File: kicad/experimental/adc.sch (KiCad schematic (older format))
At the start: 3 parts

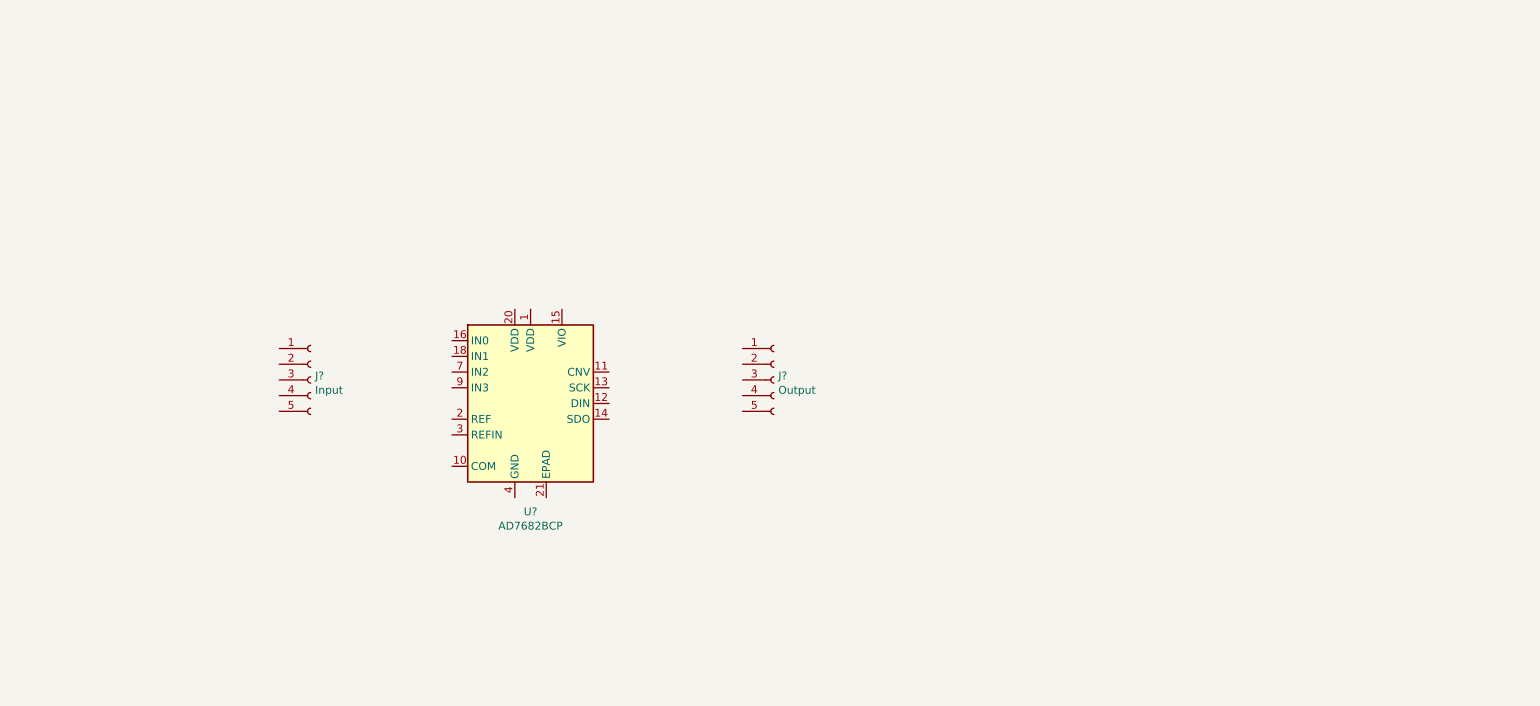
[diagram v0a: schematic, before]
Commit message: created schematic for experimental adc
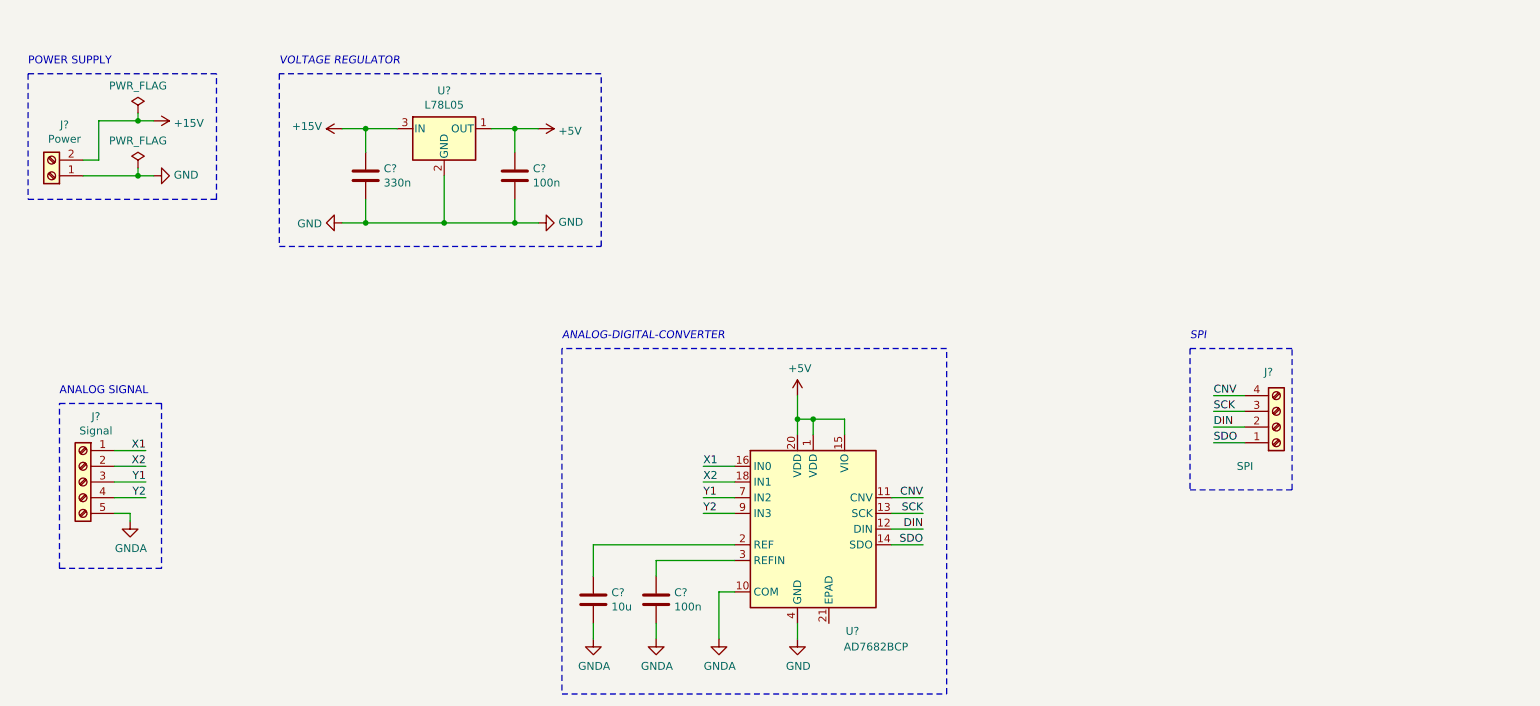
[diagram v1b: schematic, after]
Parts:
- removed J?: Input, symbol Connector:Conn_01x05_Female
- removed J?: Output, symbol Connector:Conn_01x05_Female
- added C?: 330n, symbol Device:C
- added C? (x2): 100n, symbol Device:C
- added C?: 10u, symbol Device:C
- added J?: SPI, symbol Connector:Screw_Terminal_01x04
- added J?: Signal, symbol Connector:Screw_Terminal_01x05
- added J?: Power, symbol Connector:Screw_Terminal_01x02
- added U?: L78L05, Package_TO_SOT_SMD:SOT-89-3, symbol Regulator_Linear:L78L05_SOT89
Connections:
- net +5V: now reaches U?.1 (VDD)
- net +5V: now also U?.15 (VIO), U?.20 (VDD), C?.1, U?.1 (OUT)
- net GNDA: now reaches U?.10 (COM)
- net GNDA: now also C?.2, C?.2, J?.5 (Pin_5)
- net CNV: now reaches U?.11 (CNV)
- net CNV: now also J?.4 (Pin_4)
- net DIN: now reaches U?.12 (DIN)
- net DIN: now also J?.2 (Pin_2)
- net SCK: now reaches U?.13 (SCK)
- net SCK: now also J?.3 (Pin_3)
- net SDO: now reaches U?.14 (SDO)
- net SDO: now also J?.1 (Pin_1)
- net X1: now reaches U?.16 (IN0)
- net X1: now also J?.1 (Pin_1)
- net X2: now reaches U?.18 (IN1)
- net X2: now also J?.2 (Pin_2)
- net at U?.2 (REF): now also C?.1
- net at U?.3 (REFIN): now also C?.1
- net GND: now reaches U?.4 (GND), U?.5 (GND)
- net GND: now also C?.2, C?.2, J?.1 (Pin_1), U?.2 (GND)
- net Y1: now reaches U?.7 (IN2)
- net Y1: now also J?.3 (Pin_3)
- net Y2: now reaches U?.9 (IN3)
- net Y2: now also J?.4 (Pin_4)
- new net +15V: C?.1, J?.2 (Pin_2), U?.3 (IN)
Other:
- note added: "ANALOG SIGNAL"
- note added: "ANALOG-DIGITAL-CONVERTER"
- note added: "POWER SUPPLY"
- note added: "SPI"
- note added: "VOLTAGE REGULATOR"
- moved on the sheet: U?

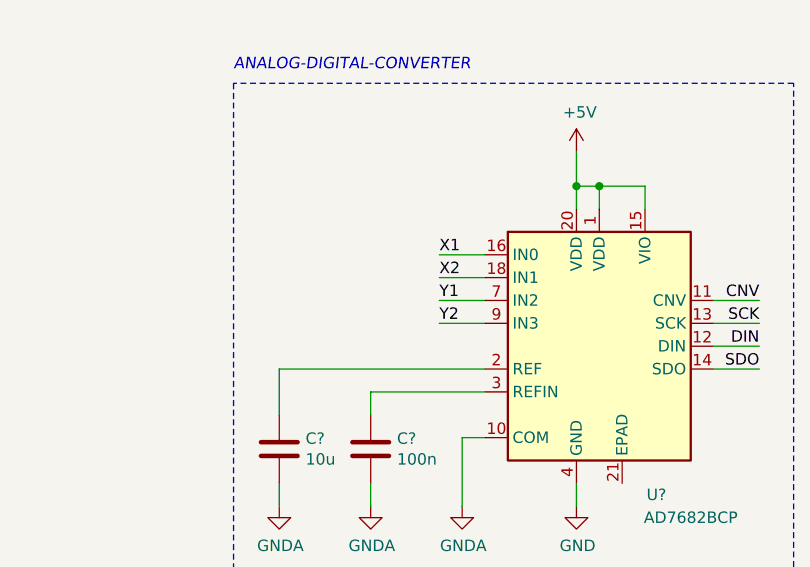
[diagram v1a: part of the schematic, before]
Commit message: added resistors to analog inputs of adc
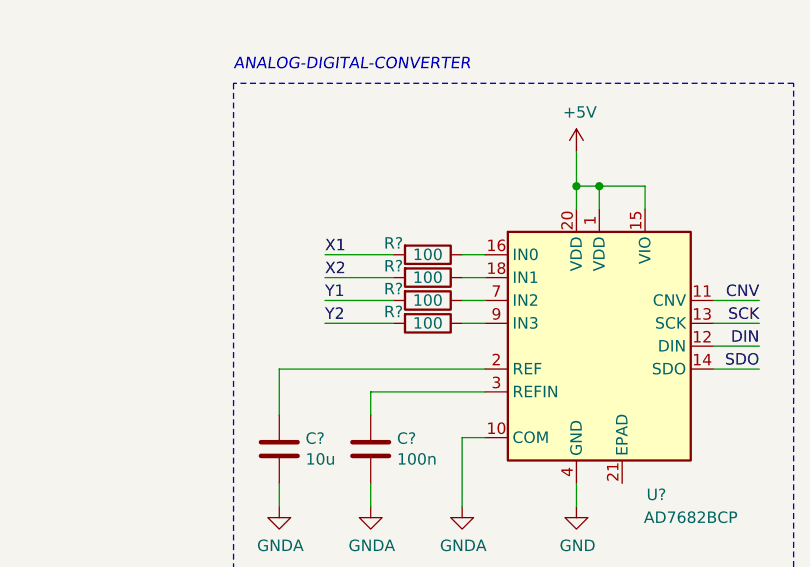
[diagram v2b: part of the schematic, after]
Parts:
- added R? (x4): 100, symbol Device:R
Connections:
- net X1: now also R?.2; no longer U?.16 (IN0)
- net X2: now also R?.2; no longer U?.18 (IN1)
- net Y1: now also R?.2; no longer U?.7 (IN2)
- net Y2: now also R?.2; no longer U?.9 (IN3)
- new net: R?.1, U?.16 (IN0)
- new net: R?.1, U?.18 (IN1)
- new net: R?.1, U?.7 (IN2)
- new net: R?.1, U?.9 (IN3)
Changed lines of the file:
@@
 EESchema Schematic File Version 4
+LIBS:experimental-cache
 EELAYER 29 0
 EELAYER END
@@
 Text Notes 8500 2950 0    50   Italic 0
 SPI
-Text Label 5400 3750 0    50   ~ 0
+Text Label 4900 3750 0    50   ~ 0
 X1
 Wire Wire Line
-	5400 3750 5600 3750
-Text Label 5400 3850 0    50   ~ 0
+	4900 3750 5200 3750
+Text Label 4900 3850 0    50   ~ 0
 X2
 Wire Wire Line
-	5400 3850 5600 3850
-Text Label 5400 3950 0    50   ~ 0
+	4900 3850 5200 3850
+Text Label 4900 3950 0    50   ~ 0
 Y1
 Wire Wire Line
-	5400 3950 5600 3950
-Text Label 5400 4050 0    50   ~ 0
+	4900 3950 5200 3950
+Text Label 4900 4050 0    50   ~ 0
 Y2
 Wire Wire Line
-	5400 4050 5600 4050
+	4900 4050 5200 4050
 Text Label 6800 3950 2    50   ~ 0
 CNV
@@
 Text Notes 4500 2950 0    50   Italic 0
 ANALOG-DIGITAL-CONVERTER
+$Comp
+L Device:R R?
+U 1 1 5D640C63
+P 5350 3750
+F 0 "R?" V 5300 3600 50  0000 C CNN
+F 1 "100" V 5350 3750 50  0000 C CNN
+F 2 "" V 5280 3750 50  0001 C CNN
+F 3 "~" H 5350 3750 50  0001 C CNN
+	1    5350 3750
+	0    1    1    0
+$EndComp
+Wire Wire Line
+	5500 3750 5600 3750
+$Comp
+L Device:R R?
+U 1 1 5D641270
+P 5350 3850
+F 0 "R?" V 5300 3700 50  0000 C CNN
+F 1 "100" V 5350 3850 50  0000 C CNN
+F 2 "" V 5280 3850 50  0001 C CNN
+F 3 "~" H 5350 3850 50  0001 C CNN
+	1    5350 3850
+	0    1    1    0
+$EndComp
+Wire Wire Line
+	5500 3850 5600 3850
+$Comp
+L Device:R R?
+U 1 1 5D6415C2
+P 5350 3950
+F 0 "R?" V 5300 3800 50  0000 C CNN
+F 1 "100" V 5350 3950 50  0000 C CNN
+F 2 "" V 5280 3950 50  0001 C CNN
+F 3 "~" H 5350 3950 50  0001 C CNN
+	1    5350 3950
+	0    1    1    0
+$EndComp
+Wire Wire Line
+	5500 3950 5600 3950
+$Comp
+L Device:R R?
+U 1 1 5D6417EE
+P 5350 4050
+F 0 "R?" V 5300 3900 50  0000 C CNN
+F 1 "100" V 5350 4050 50  0000 C CNN
+F 2 "" V 5280 4050 50  0001 C CNN
+F 3 "~" H 5350 4050 50  0001 C CNN
+	1    5350 4050
+	0    1    1    0
+$EndComp
+Wire Wire Line
+	5500 4050 5600 4050
 $EndSCHEMATC

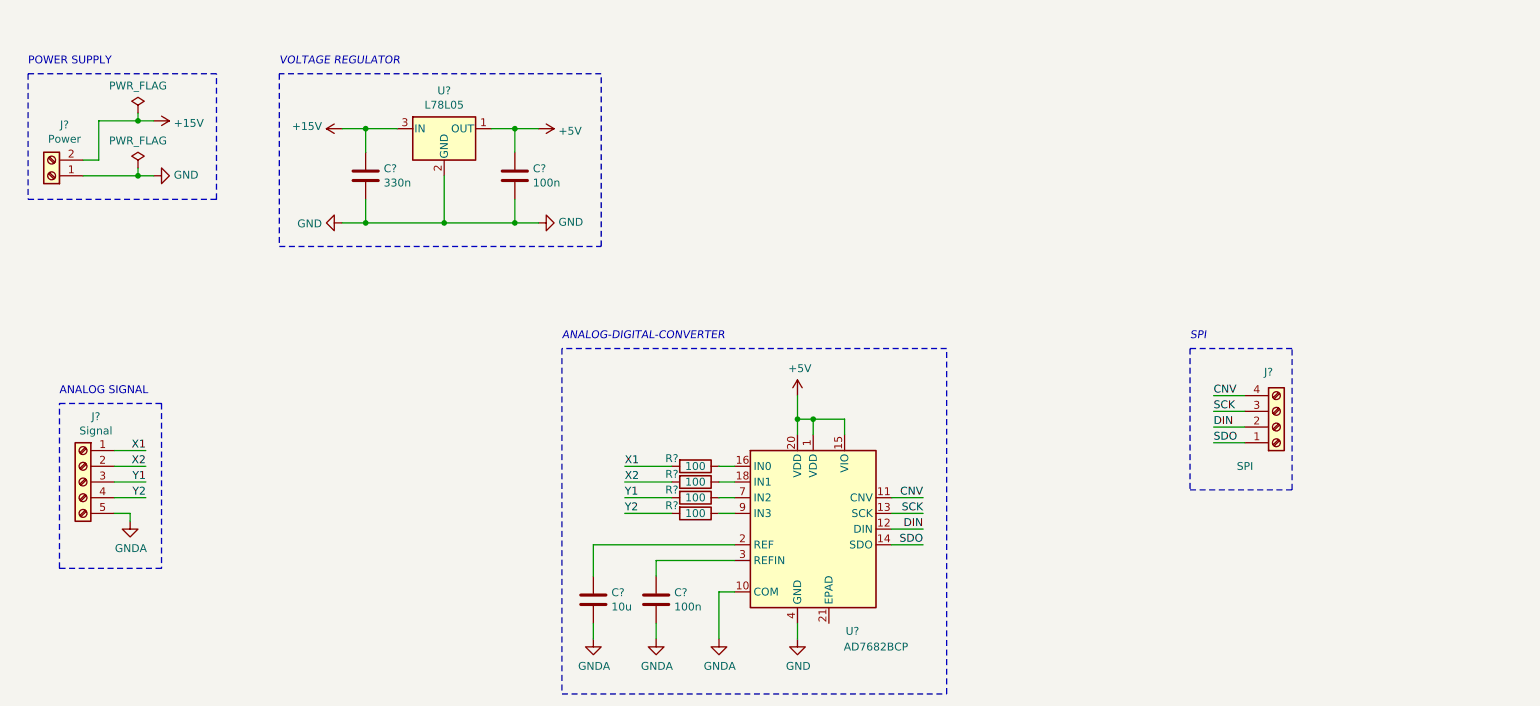
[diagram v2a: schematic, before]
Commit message: added test points to experimental adc and buffer boards, improved schematic, assigned footprints
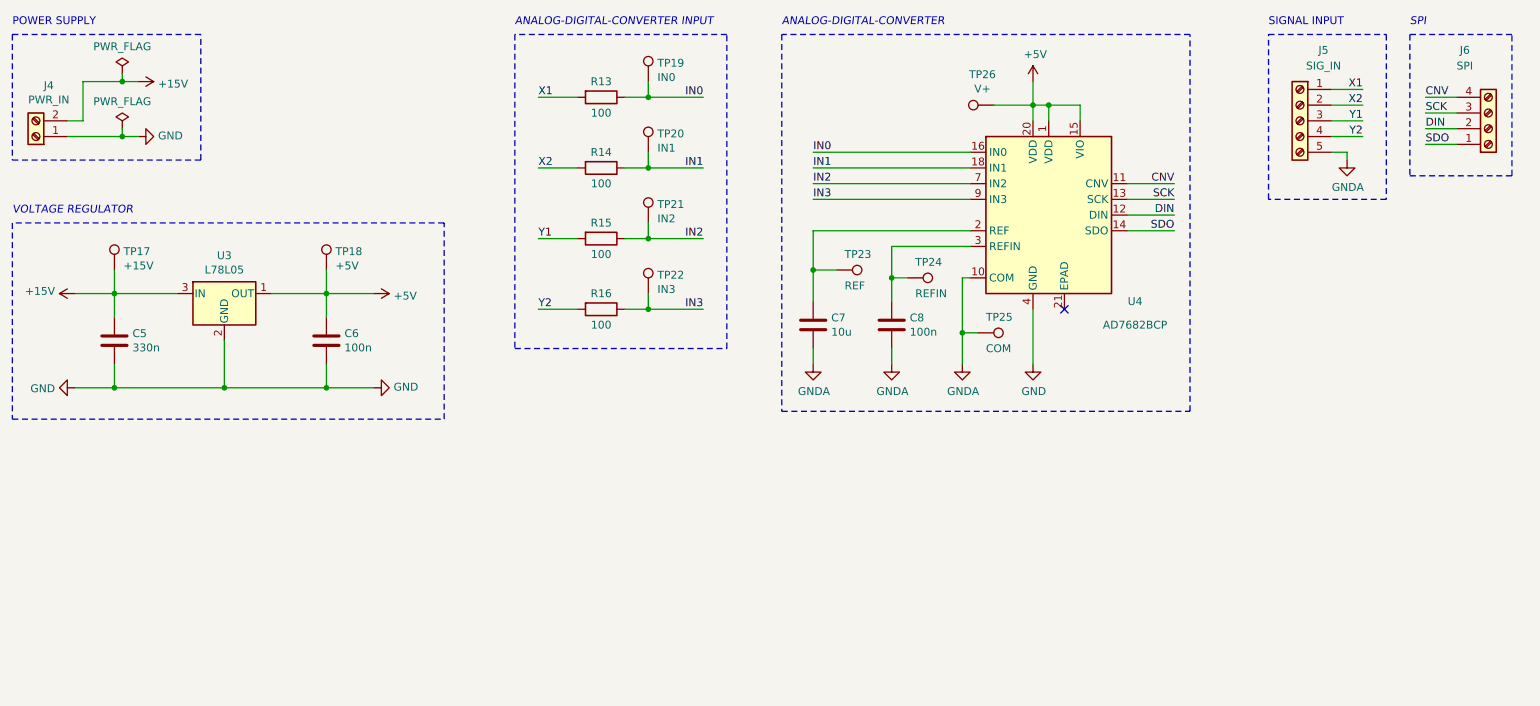
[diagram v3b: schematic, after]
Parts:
- added TP17: +15V, TestPoint:TestPoint_THTPad_1.0x1.0mm_Drill0.5mm, symbol Connector:TestPoint
- added TP18: +5V, TestPoint:TestPoint_THTPad_1.0x1.0mm_Drill0.5mm, symbol Connector:TestPoint
- added TP19: IN0, TestPoint:TestPoint_THTPad_1.0x1.0mm_Drill0.5mm, symbol Connector:TestPoint
- added TP20: IN1, TestPoint:TestPoint_THTPad_1.0x1.0mm_Drill0.5mm, symbol Connector:TestPoint
- added TP21: IN2, TestPoint:TestPoint_THTPad_1.0x1.0mm_Drill0.5mm, symbol Connector:TestPoint
- added TP22: IN3, TestPoint:TestPoint_THTPad_1.0x1.0mm_Drill0.5mm, symbol Connector:TestPoint
- added TP23: REF, TestPoint:TestPoint_THTPad_1.0x1.0mm_Drill0.5mm, symbol Connector:TestPoint
- added TP24: REFIN, TestPoint:TestPoint_THTPad_1.0x1.0mm_Drill0.5mm, symbol Connector:TestPoint
- added TP25: COM, TestPoint:TestPoint_THTPad_1.0x1.0mm_Drill0.5mm, symbol Connector:TestPoint
- added TP26: V+, TestPoint:TestPoint_THTPad_1.0x1.0mm_Drill0.5mm, symbol Connector:TestPoint
- C5, C6, C7, C8: renamed from C?; footprint (none) -> Capacitor_SMD:C_0603_1608Metric
- J4: renamed from J?; value Power -> PWR_IN; footprint (none) -> TerminalBlock_TE-Connectivity:TerminalBlock_TE_282834-2_1x02_P2.54mm_Horizontal
- J5: renamed from J?; value Signal -> SIG_IN; footprint (none) -> TerminalBlock_TE-Connectivity:TerminalBlock_TE_282834-5_1x05_P2.54mm_Horizontal
- J6: renamed from J?; footprint (none) -> TerminalBlock_TE-Connectivity:TerminalBlock_TE_282834-4_1x04_P2.54mm_Horizontal
- R13, R14, R15, R16: renamed from R?; footprint (none) -> Resistor_SMD:R_0603_1608Metric
- gave numbers to parts that had none: 2
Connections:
- net +15V: now also TP17.1
- net +5V: now also TP18.1, TP26.1
- net GNDA: now also TP25.1
- net IN0: now reaches R13.1, U4.16 (IN0)
- net IN0: now also TP19.1
- net IN1: now reaches R14.1, U4.18 (IN1)
- net IN1: now also TP20.1
- net at C7.1, U4.2 (REF): now also TP23.1
- net at C8.1, U4.3 (REFIN): now also TP24.1
- net IN2: now reaches R15.1, U4.7 (IN2)
- net IN2: now also TP21.1
- net IN3: now reaches R16.1, U4.9 (IN3)
- net IN3: now also TP22.1
- no-connect marks 0 -> 1
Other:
- note added: "ANALOG-DIGITAL-CONVERTER INPUT\n"
- note added: "SIGNAL INPUT"
- note removed: "ANALOG SIGNAL"
- moved on the sheet: C5, C6, C7, C8, J4, J5, J6, R13, R14, R15, R16, U3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

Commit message: designed pcb for experimental buffer board
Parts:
- TP17, TP18, TP19, TP20, TP21, TP22, TP23, TP24, TP25, TP26: footprint TestPoint:TestPoint_THTPad_1.0x1.0mm_Drill0.5mm -> TestPoint:TestPoint_THTPad_D1.0mm_Drill0.5mm
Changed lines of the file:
@@
 F 0 "TP17" H 1708 2618 50  0000 L CNN
 F 1 "+15V" H 1708 2527 50  0000 L CNN
-F 2 "TestPoint:TestPoint_THTPad_1.0x1.0mm_Drill0.5mm" H 1850 2500 50  0001 C CNN
+F 2 "TestPoint:TestPoint_THTPad_D1.0mm_Drill0.5mm" H 1850 2500 50  0001 C CNN
 F 3 "~" H 1850 2500 50  0001 C CNN
 	1    1650 2500
@@
 F 0 "TP18" H 3058 2618 50  0000 L CNN
 F 1 "+5V" H 3058 2527 50  0000 L CNN
-F 2 "TestPoint:TestPoint_THTPad_1.0x1.0mm_Drill0.5mm" H 3200 2500 50  0001 C CNN
+F 2 "TestPoint:TestPoint_THTPad_D1.0mm_Drill0.5mm" H 3200 2500 50  0001 C CNN
 F 3 "~" H 3200 2500 50  0001 C CNN
 	1    3000 2500
@@
 F 0 "TP19" H 5108 1418 50  0000 L CNN
 F 1 "IN0" H 5108 1327 50  0000 L CNN
-F 2 "TestPoint:TestPoint_THTPad_1.0x1.0mm_Drill0.5mm" H 5250 1300 50  0001 C CNN
+F 2 "TestPoint:TestPoint_THTPad_D1.0mm_Drill0.5mm" H 5250 1300 50  0001 C CNN
 F 3 "~" H 5250 1300 50  0001 C CNN
 	1    5050 1300
@@
 F 0 "TP20" H 5108 1868 50  0000 L CNN
 F 1 "IN1" H 5108 1777 50  0000 L CNN
-F 2 "TestPoint:TestPoint_THTPad_1.0x1.0mm_Drill0.5mm" H 5250 1750 50  0001 C CNN
+F 2 "TestPoint:TestPoint_THTPad_D1.0mm_Drill0.5mm" H 5250 1750 50  0001 C CNN
 F 3 "~" H 5250 1750 50  0001 C CNN
 	1    5050 1750
@@
 F 0 "TP21" H 5108 2318 50  0000 L CNN
 F 1 "IN2" H 5108 2227 50  0000 L CNN
-F 2 "TestPoint:TestPoint_THTPad_1.0x1.0mm_Drill0.5mm" H 5250 2200 50  0001 C CNN
+F 2 "TestPoint:TestPoint_THTPad_D1.0mm_Drill0.5mm" H 5250 2200 50  0001 C CNN
 F 3 "~" H 5250 2200 50  0001 C CNN
 	1    5050 2200
@@
 F 0 "TP22" H 5108 2768 50  0000 L CNN
 F 1 "IN3" H 5108 2677 50  0000 L CNN
-F 2 "TestPoint:TestPoint_THTPad_1.0x1.0mm_Drill0.5mm" H 5250 2650 50  0001 C CNN
+F 2 "TestPoint:TestPoint_THTPad_D1.0mm_Drill0.5mm" H 5250 2650 50  0001 C CNN
 F 3 "~" H 5250 2650 50  0001 C CNN
 	1    5050 2650
@@
 F 0 "TP26" V 7445 1522 50  0000 C CNN
 F 1 "V+" V 7354 1522 50  0000 C CNN
-F 2 "TestPoint:TestPoint_THTPad_1.0x1.0mm_Drill0.5mm" H 7450 1450 50  0001 C CNN
+F 2 "TestPoint:TestPoint_THTPad_D1.0mm_Drill0.5mm" H 7450 1450 50  0001 C CNN
 F 3 "~" H 7450 1450 50  0001 C CNN
 	1    7250 1450
@@
 F 0 "TP25" V 7050 2950 50  0000 L CNN
 F 1 "COM" V 7250 2950 50  0000 L CNN
-F 2 "TestPoint:TestPoint_THTPad_1.0x1.0mm_Drill0.5mm" H 7350 2900 50  0001 C CNN
+F 2 "TestPoint:TestPoint_THTPad_D1.0mm_Drill0.5mm" H 7350 2900 50  0001 C CNN
 F 3 "~" H 7350 2900 50  0001 C CNN
 	1    7150 2900
@@
 F 0 "TP24" V 6600 2600 50  0000 L CNN
 F 1 "REFIN" V 6800 2600 50  0000 L CNN
-F 2 "TestPoint:TestPoint_THTPad_1.0x1.0mm_Drill0.5mm" H 6900 2550 50  0001 C CNN
+F 2 "TestPoint:TestPoint_THTPad_D1.0mm_Drill0.5mm" H 6900 2550 50  0001 C CNN
 F 3 "~" H 6900 2550 50  0001 C CNN
 	1    6700 2550
@@
 F 0 "TP23" V 6150 2550 50  0000 L CNN
 F 1 "REF" V 6350 2550 50  0000 L CNN
-F 2 "TestPoint:TestPoint_THTPad_1.0x1.0mm_Drill0.5mm" H 6450 2500 50  0001 C CNN
+F 2 "TestPoint:TestPoint_THTPad_D1.0mm_Drill0.5mm" H 6450 2500 50  0001 C CNN
 F 3 "~" H 6450 2500 50  0001 C CNN
 	1    6250 2500
